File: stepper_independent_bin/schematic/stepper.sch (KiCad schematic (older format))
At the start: 15 parts, among them J1 DB25, P1 CONN_14, P2 CONN_4, P3 CONN_14, P4 CONN_5, SW1 SW_PUSH, U1 STM8S105K4T6C

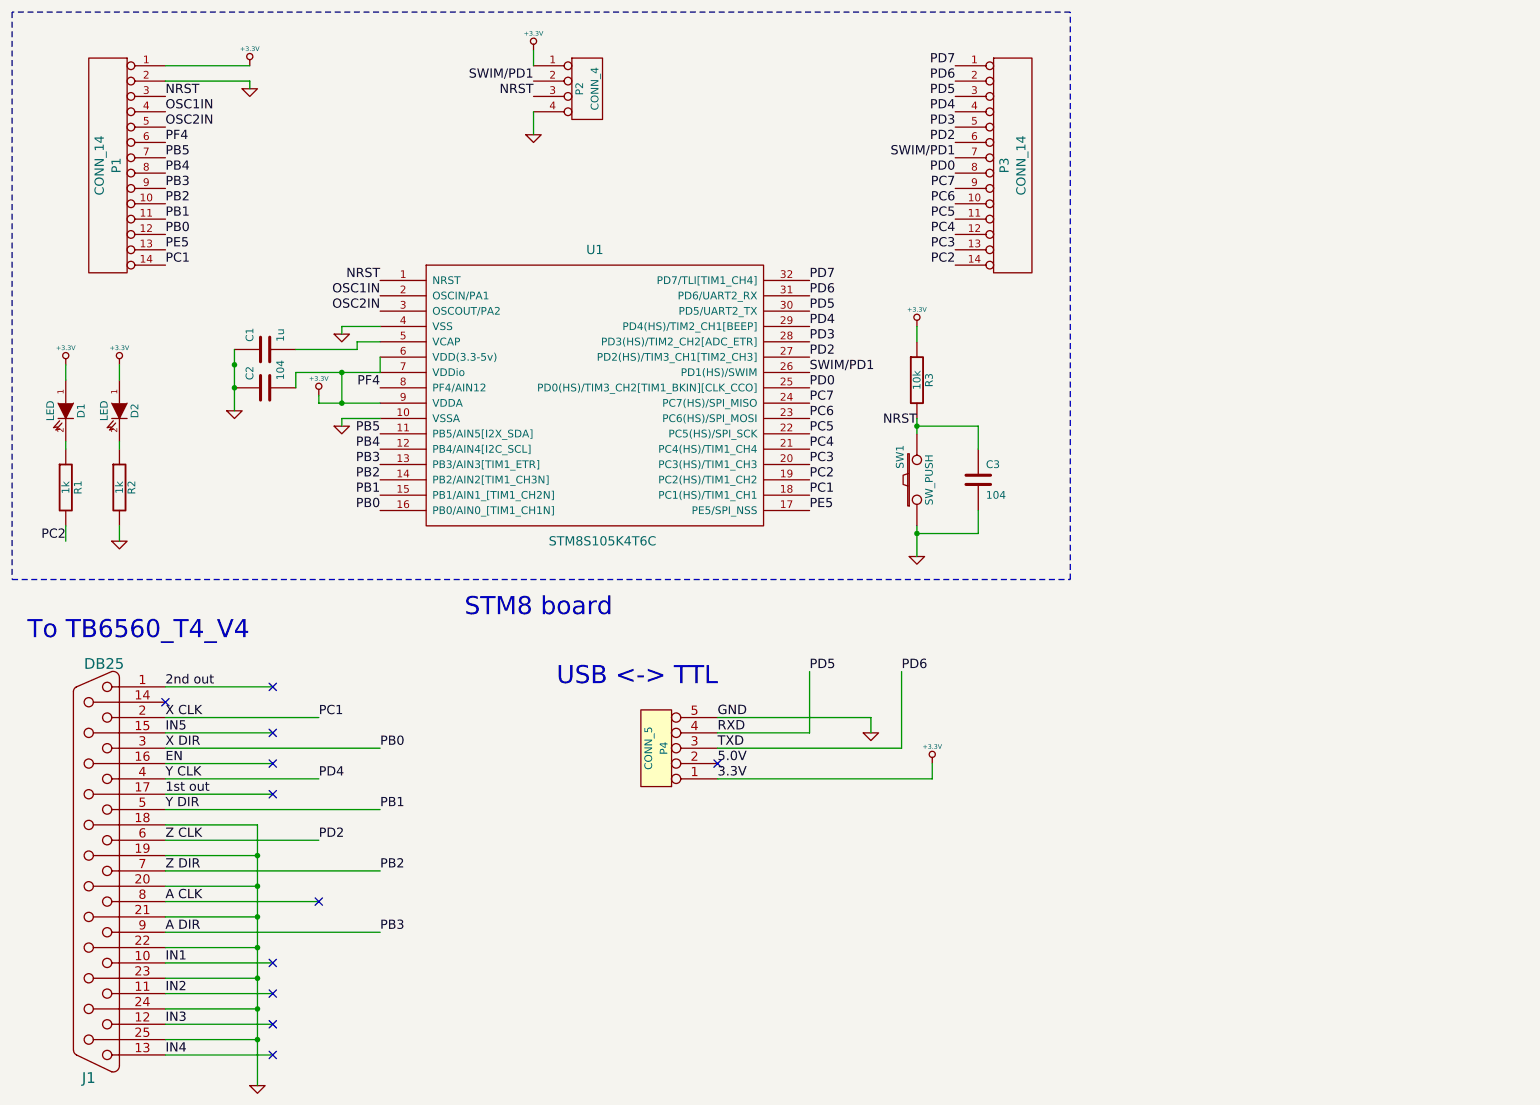
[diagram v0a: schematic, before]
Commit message: now we can manage a lot of stepper motors by a lot of MCUs on one UART bus
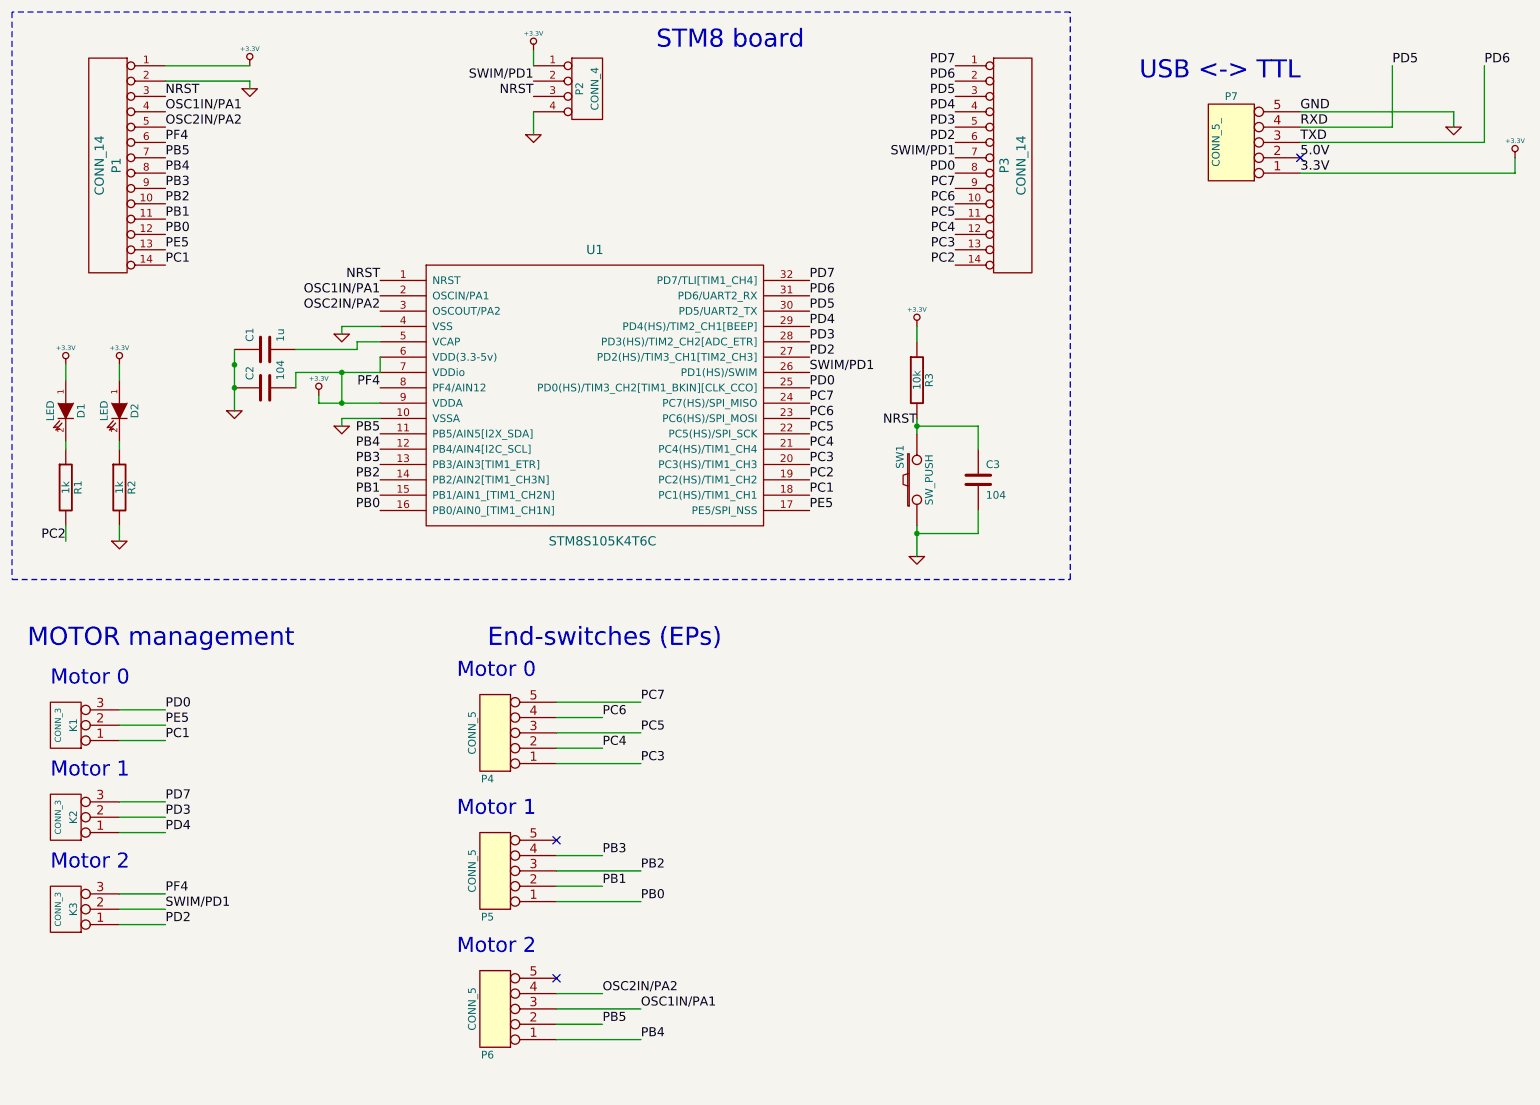
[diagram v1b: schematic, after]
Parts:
- removed J1: DB25, symbol DB25
- added K1, K2, K3: CONN_3, symbol CONN_3
- added P5, P6: CONN_5, symbol CONN_5
- added P7: CONN_5_, symbol CONN_5_
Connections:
- net +3.3V: now also P7.1; no longer P4.1
- net 5.0V: now also P7.2; no longer P4.2
- net GND: now also P7.5; no longer P4.5
- net PB0: now also P5.1
- net PB1: now also P5.2
- net PB2: now also P5.3
- net PB4: now also P6.1
- net PB5: now also P6.2
- net PC1: now also K1.1 (P1)
- net PC3: now also P4.1
- net PC4: now also P4.2
- net PC5: now also P4.3
- net PC6: now also P4.4
- net PC7: now also P4.5
- net PD0: now also K1.3 (P3)
- net PD2: now also K3.1 (P1)
- net PD3: now also K2.2 (PM)
- net PD4: now also K2.1 (P1)
- net PD5: now also P7.4; no longer P4.4
- net PD6: now also P7.3; no longer P4.3
- net PD7: now also K2.3 (P3)
- net PE5: now also K1.2 (PM)
- net PF4: now also K3.3 (P3)
- net SWIM/PD1: now also K3.2 (PM)
- net A DIR renamed PB3
- net PB3: now also P5.4
- net OSC1IN renamed OSC1IN/PA1
- net OSC1IN/PA1: now also P6.3
- net OSC2IN renamed OSC2IN/PA2
- net OSC2IN/PA2: now also P6.4
- no-connect marks 11 -> 3
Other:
- note added: "End-switches (EPs)"
- note added: "MOTOR management"
- note added: "Motor 0"
- note added: "Motor 1"
- note added: "Motor 2"
- note removed: "To TB6560_T4_V4"

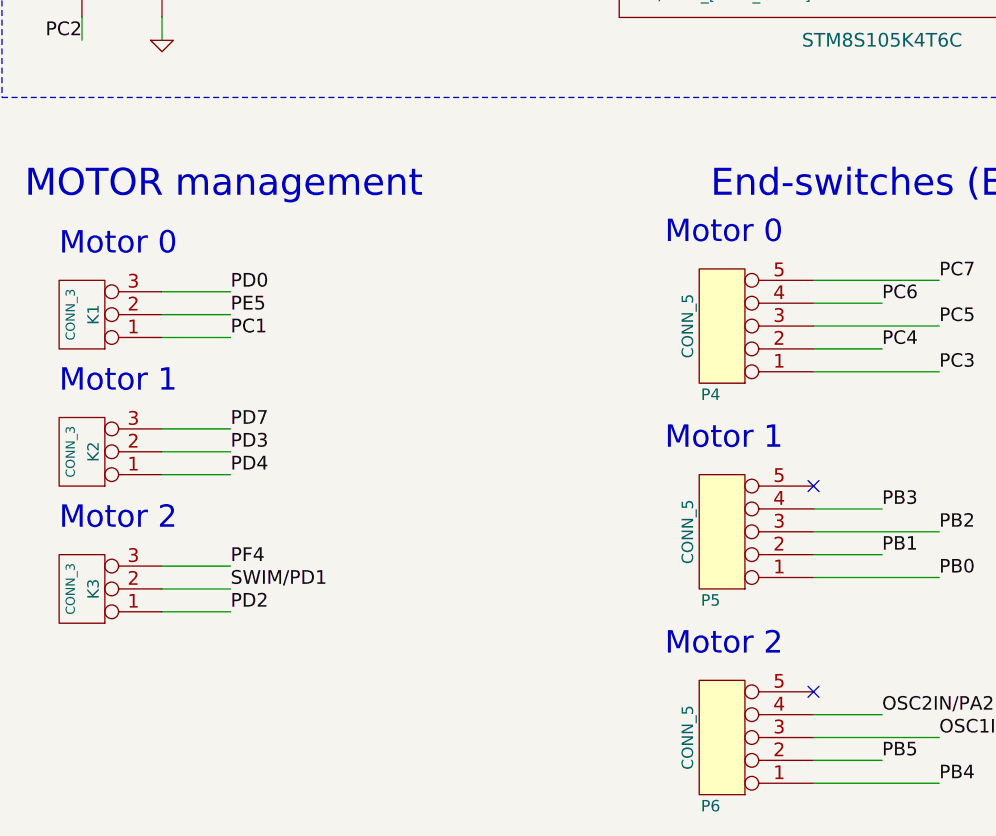
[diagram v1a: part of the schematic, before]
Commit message: Fixed some other bugs, EN now inverted
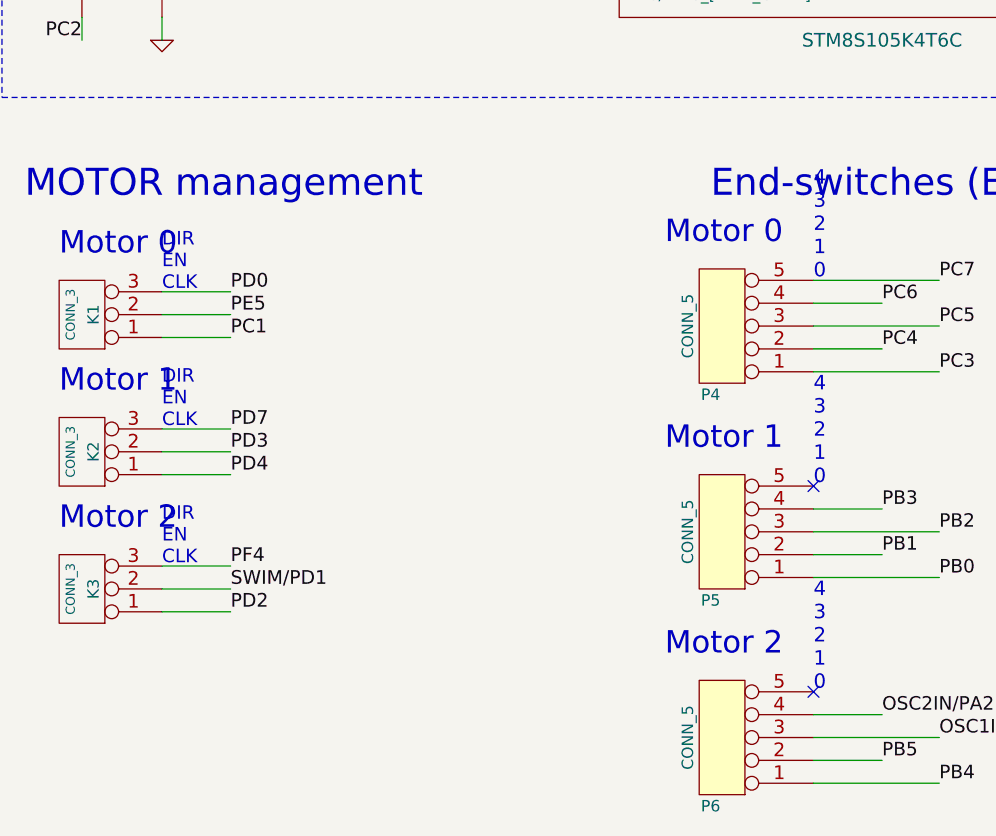
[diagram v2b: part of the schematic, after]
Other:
- note added: "4\n3\n2\n1\n0"
- note added: "DIR\nEN\nCLK"
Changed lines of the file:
@@
-EESchema Schematic File Version 2  date Ср 26 фев 2014 17:52:34
+EESchema Schematic File Version 2  date Пн 03 мар 2014 17:27:22
 LIBS:power
 LIBS:device
@@
 LIBS:stm8s105k4t6c
 LIBS:stepper-cache
+LIBS:stepper-cache
 EELAYER 27 0
 EELAYER END
@@
 Sheet 1 1
 Title ""
-Date "26 feb 2014"
+Date "3 mar 2014"
 Rev ""
 Comp ""
@@
 PB4
 NoConn ~ 4150 6800
+Text Notes 1300 5050 0    59   ~ 0
+DIR\nEN\nCLK
+Text Notes 1300 5650 0    59   ~ 0
+DIR\nEN\nCLK
+Text Notes 1300 6250 0    59   ~ 0
+DIR\nEN\nCLK
+Text Notes 4150 5000 0    63   ~ 0
+4\n3\n2\n1\n0
+Text Notes 4150 5900 0    63   ~ 0
+4\n3\n2\n1\n0
+Text Notes 4150 6800 0    63   ~ 0
+4\n3\n2\n1\n0
 $EndSCHEMATC
